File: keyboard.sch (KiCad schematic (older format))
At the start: 34 parts, among them J1 USB_C_Receptacle_USB2.0, J2 -, J3 -, K1 SW, K2 SW, P1 SWD, P2 BATT, P3 BATT, U1 nRF52810-ND04C, U2 CH554T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

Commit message: 更新部分cache的库
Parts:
- R1, R101, R102, R103, R2, R3, R4, R5, R6: symbol keyboard-rescue:R_Small-RESCUE-ble4100-nrf-ble4100-nrf-rescue -> Device:R_Small
- U2: symbol keyboard-rescue:CH554T-ch554t -> custom:CH554T
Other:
- moved on the sheet: C1, C2, J1, K1, P1, R1, R5, R6

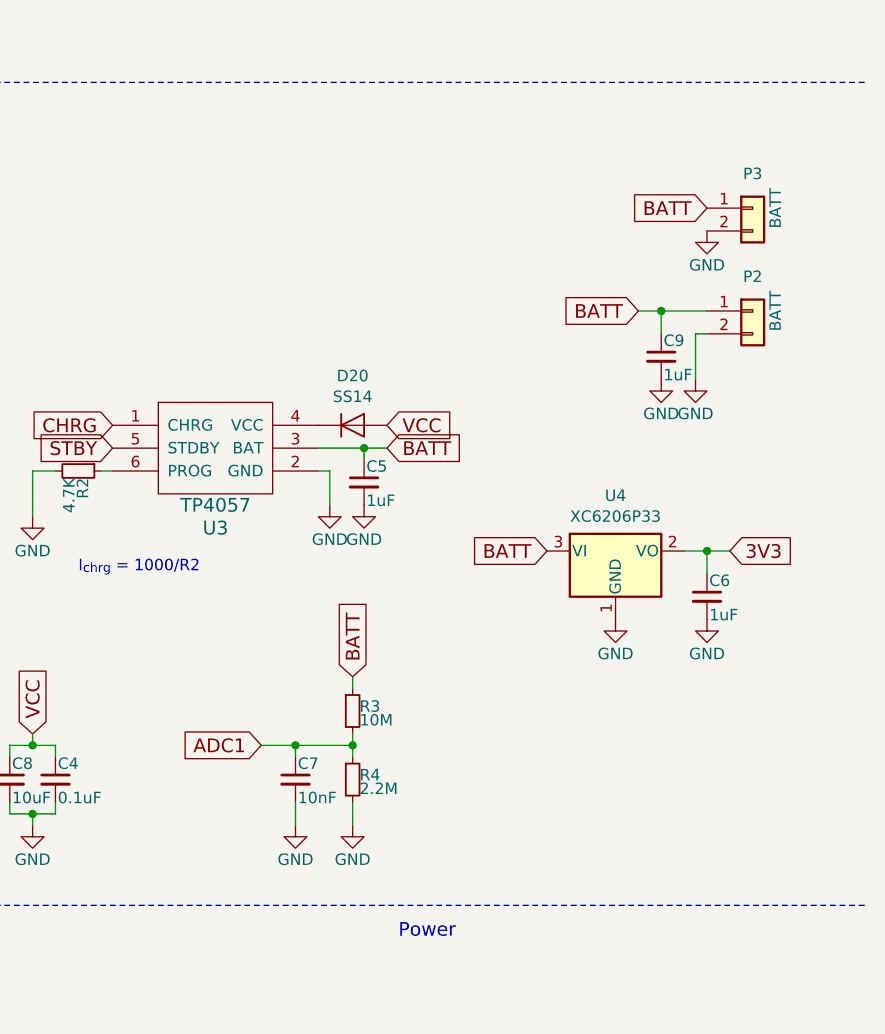
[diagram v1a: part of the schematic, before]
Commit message: 改进供电部分，现在支持仅USB供电了
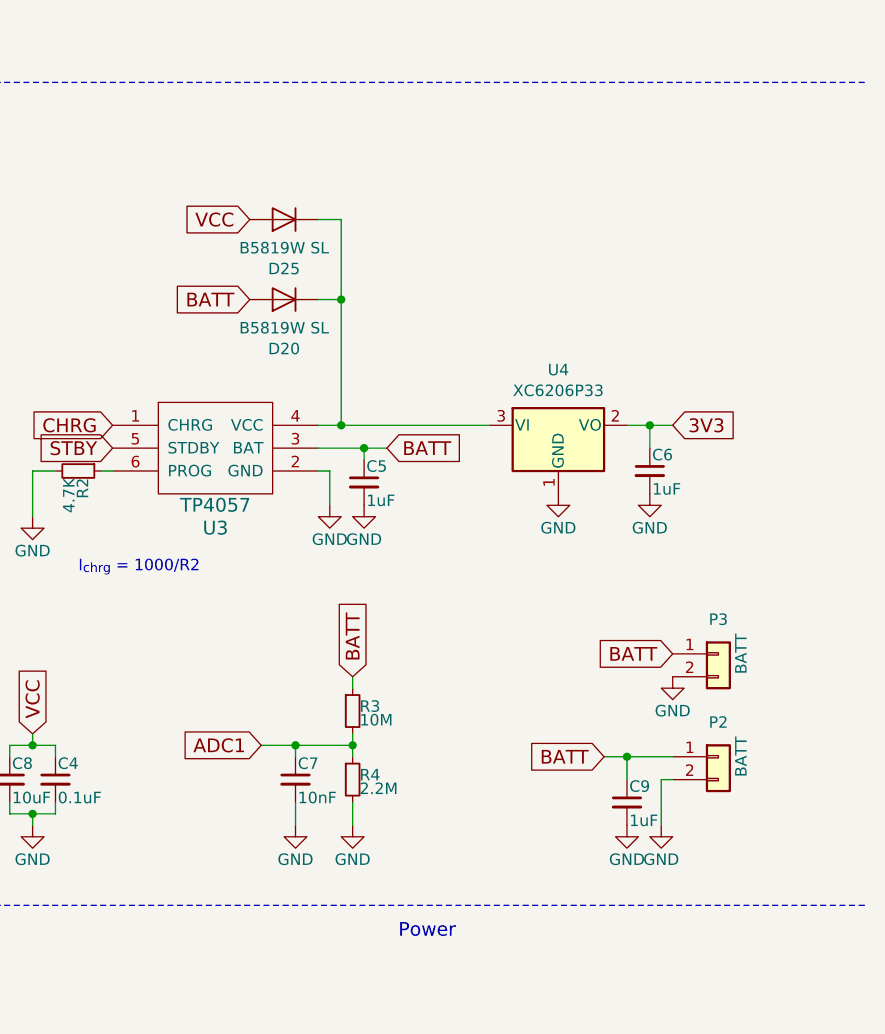
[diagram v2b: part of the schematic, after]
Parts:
- added D25: B5819W SL, Diode_SMD:D_SOD-123, symbol Device:D
- D20: value SS14 -> B5819W SL; footprint Diode_SMD:D_SMA -> Diode_SMD:D_SOD-123
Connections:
- net BATT: now also D20.2 (A); no longer U4.3 (VI)
- net VCC: now also D25.2 (A); no longer D20.2 (A)
- net at D20.1 (K), U3.4 (VCC): now also U4.3 (VI), D25.1 (K)
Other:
- moved on the sheet: C6, C9, D20, P2, P3, U4
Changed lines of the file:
@@
 L Connector_Generic:Conn_01x02 P2
 U 1 1 5867EF56
-P 10700 3700
-F 0 "P2" H 10700 3850 50  0000 C CNN
-F 1 "BATT" V 10800 3700 50  0000 C CNN
-F 2 "Connector_PinHeader_2.54mm:PinHeader_1x02_P2.54mm_Vertical" H 10700 3700 50  0001 C CNN
-F 3 "" H 10700 3700 50  0000 C CNN
-	1    10700 3700
+P 10550 5650
+F 0 "P2" H 10550 5800 50  0000 C CNN
+F 1 "BATT" V 10650 5650 50  0000 C CNN
+F 2 "Connector_PinHeader_2.54mm:PinHeader_1x02_P2.54mm_Vertical" H 10550 5650 50  0001 C CNN
+F 3 "" H 10550 5650 50  0000 C CNN
+	1    10550 5650
 	1    0    0    -1
 $EndComp
@@
 L power:GND #PWR017
 U 1 1 58688C41
-P 10450 4000
-F 0 "#PWR017" H 10450 3750 50  0001 C CNN
-F 1 "GND" H 10450 3850 50  0000 C CNN
-F 2 "" H 10450 4000 50  0000 C CNN
-F 3 "" H 10450 4000 50  0000 C CNN
-	1    10450 4000
+P 10300 5950
+F 0 "#PWR017" H 10300 5700 50  0001 C CNN
+F 1 "GND" H 10300 5800 50  0000 C CNN
+F 2 "" H 10300 5950 50  0000 C CNN
+F 3 "" H 10300 5950 50  0000 C CNN
+	1    10300 5950
 	1    0    0    -1
 $EndComp
 Text GLabel 9100 4300 2    60   Input ~ 0
 BATT
-Text GLabel 10200 3700 0    60   Input ~ 0
+Text GLabel 10050 5650 0    60   Input ~ 0
 BATT
 Text GLabel 1300 4650 2    60   Input ~ 0
@@
 L Device:C_Small C6
 U 1 1 58689C99
-P 10500 4950
-F 0 "C6" H 10510 5020 50  0000 L CNN
-F 1 "1uF" H 10510 4870 50  0000 L CNN
-F 2 "Capacitor_SMD:C_0805_2012Metric" H 10500 4950 50  0001 C CNN
-F 3 "~" H 10500 4950 50  0000 C CNN
-	1    10500 4950
+P 10250 4400
+F 0 "C6" H 10260 4470 50  0000 L CNN
+F 1 "1uF" H 10260 4320 50  0000 L CNN
+F 2 "Capacitor_SMD:C_0805_2012Metric" H 10250 4400 50  0001 C CNN
+F 3 "~" H 10250 4400 50  0000 C CNN
+	1    10250 4400
 	1    0    0    -1
 $EndComp
@@
 Text Notes 9150 6450 0    60   ~ 0
 Power
-Text GLabel 9100 4200 2    60   Input ~ 0
+Text GLabel 8500 3300 0    60   Input ~ 0
 VCC
 Text GLabel 7550 5550 1    60   Input ~ 0
@@
 	8850 4400 8850 4550
 Wire Wire Line
-	10500 3800 10450 3800
-Wire Wire Line
-	10450 3800 10450 4000
+	10350 5750 10300 5750
+Wire Wire Line
+	10300 5750 10300 5950
 Wire Wire Line
 	1300 4350 1400 4350
@@
 L Regulator_Linear:AP2127N-3.0 U4
 U 1 1 5AE6D677
-P 10100 4750
-F 0 "U4" H 10100 4992 50  0000 C CNN
-F 1 "XC6206P33" H 10100 4901 50  0000 C CNN
-F 2 "Package_TO_SOT_SMD:SOT-23" H 10100 4975 50  0001 C CIN
-F 3 "https://www.diodes.com/assets/Datasheets/AP2127.pdf" H 10100 4750 50  0001 C CNN
-	1    10100 4750
-	1    0    0    -1
-$EndComp
-Text GLabel 9800 4750 0    60   Input ~ 0
-BATT
-Text GLabel 10600 4750 2    60   Input ~ 0
+P 9850 4200
+F 0 "U4" H 9850 4442 50  0000 C CNN
+F 1 "XC6206P33" H 9850 4351 50  0000 C CNN
+F 2 "Package_TO_SOT_SMD:SOT-23" H 9850 4425 50  0001 C CIN
+F 3 "https://www.diodes.com/assets/Datasheets/AP2127.pdf" H 9850 4200 50  0001 C CNN
+	1    9850 4200
+	1    0    0    -1
+$EndComp
+Text GLabel 10350 4200 2    60   Input ~ 0
 3V3
 $Comp
 L power:GND #PWR016
 U 1 1 5AE6D8BF
-P 10100 5050
-F 0 "#PWR016" H 10100 4800 50  0001 C CNN
-F 1 "GND" H 10100 4900 50  0000 C CNN
-F 2 "" H 10100 5050 50  0000 C CNN
-F 3 "" H 10100 5050 50  0000 C CNN
-	1    10100 5050
+P 9850 4500
+F 0 "#PWR016" H 9850 4250 50  0001 C CNN
+F 1 "GND" H 9850 4350 50  0000 C CNN
+F 2 "" H 9850 4500 50  0000 C CNN
+F 3 "" H 9850 4500 50  0000 C CNN
+	1    9850 4500
 	1    0    0    -1
 $EndComp
@@
 L Device:D D20
 U 1 1 5AFFEAFC
-P 8950 4200
-F 0 "D20" H 8950 4416 50  0000 C CNN
-F 1 "SS14" H 8950 4325 50  0000 C CNN
-F 2 "Diode_SMD:D_SMA" H 8950 4200 50  0001 C CNN
-F 3 "~" H 8950 4200 50  0001 C CNN
-	1    8950 4200
-	1    0    0    -1
+P 8650 3650
+F 0 "D20" H 8650 3866 50  0000 C CNN
+F 1 "B5819W SL" H 8650 3775 50  0000 C CNN
+F 2 "Diode_SMD:D_SOD-123" H 8650 3650 50  0001 C CNN
+F 3 "~" H 8650 3650 50  0001 C CNN
+	1    8650 3650
+	-1   0    0    1
 $EndComp
 Text GLabel 2800 4100 2    60   Input ~ 0
@@
 L power:GND #PWR023
 U 1 1 5CC46D5E
-P 10500 5050
-F 0 "#PWR023" H 10500 4800 50  0001 C CNN
-F 1 "GND" H 10500 4900 50  0000 C CNN
-F 2 "" H 10500 5050 50  0000 C CNN
-F 3 "" H 10500 5050 50  0000 C CNN
-	1    10500 5050
-	1    0    0    -1
-$EndComp
-Wire Wire Line
-	10400 4750 10500 4750
-Wire Wire Line
-	10500 4850 10500 4750
-Connection ~ 10500 4750
-Wire Wire Line
-	10500 4750 10600 4750
+P 10250 4500
+F 0 "#PWR023" H 10250 4250 50  0001 C CNN
+F 1 "GND" H 10250 4350 50  0000 C CNN
+F 2 "" H 10250 4500 50  0000 C CNN
+F 3 "" H 10250 4500 50  0000 C CNN
+	1    10250 4500
+	1    0    0    -1
+$EndComp
+Wire Wire Line
+	10150 4200 10250 4200
+Wire Wire Line
+	10250 4300 10250 4200
+Connection ~ 10250 4200
+Wire Wire Line
+	10250 4200 10350 4200
 Wire Wire Line
 	8800 4300 9000 4300
@@
 $EndComp
 Wire Wire Line
-	10500 3700 10300 3700
+	10350 5650 10150 5650
 $Comp
 L Device:C_Small C9
 U 1 1 5CD13C66
-P 10300 3900
-F 0 "C9" H 10310 3970 50  0000 L CNN
-F 1 "1uF" H 10310 3820 50  0000 L CNN
-F 2 "Capacitor_SMD:C_0805_2012Metric" H 10300 3900 50  0001 C CNN
-F 3 "~" H 10300 3900 50  0000 C CNN
-	1    10300 3900
-	1    0    0    -1
-$EndComp
-Wire Wire Line
-	10300 3800 10300 3700
-Connection ~ 10300 3700
-Wire Wire Line
-	10300 3700 10200 3700
+P 10150 5850
+F 0 "C9" H 10160 5920 50  0000 L CNN
+F 1 "1uF" H 10160 5770 50  0000 L CNN
+F 2 "Capacitor_SMD:C_0805_2012Metric" H 10150 5850 50  0001 C CNN
+F 3 "~" H 10150 5850 50  0000 C CNN
+	1    10150 5850
+	1    0    0    -1
+$EndComp
+Wire Wire Line
+	10150 5750 10150 5650
+Connection ~ 10150 5650
+Wire Wire Line
+	10150 5650 10050 5650
 $Comp
 L power:GND #PWR012
 U 1 1 5CD4AD12
-P 10300 4000
-F 0 "#PWR012" H 10300 3750 50  0001 C CNN
-F 1 "GND" H 10300 3850 50  0000 C CNN
-F 2 "" H 10300 4000 50  0000 C CNN
-F 3 "" H 10300 4000 50  0000 C CNN
-	1    10300 4000
+P 10150 5950
+F 0 "#PWR012" H 10150 5700 50  0001 C CNN
+F 1 "GND" H 10150 5800 50  0000 C CNN
+F 2 "" H 10150 5950 50  0000 C CNN
+F 3 "" H 10150 5950 50  0000 C CNN
+	1    10150 5950
 	1    0    0    -1
 $EndComp
@@
 L Connector_Generic:Conn_01x02 P3
 U 1 1 5D6C74C7
-P 10700 3250
-F 0 "P3" H 10700 3400 50  0000 C CNN
-F 1 "BATT" V 10800 3250 50  0000 C CNN
-F 2 "Connector_PinSocket_2.00mm:PinSocket_1x02_P2.00mm_Vertical" H 10700 3250 50  0001 C CNN
-F 3 "" H 10700 3250 50  0000 C CNN
-	1    10700 3250
-	1    0    0    -1
-$EndComp
-Text GLabel 10500 3250 0    60   Input ~ 0
+P 10550 5200
+F 0 "P3" H 10550 5350 50  0000 C CNN
+F 1 "BATT" V 10650 5200 50  0000 C CNN
+F 2 "Connector_PinSocket_2.00mm:PinSocket_1x02_P2.00mm_Vertical" H 10550 5200 50  0001 C CNN
+F 3 "" H 10550 5200 50  0000 C CNN
+	1    10550 5200
+	1    0    0    -1
+$EndComp
+Text GLabel 10350 5200 0    60   Input ~ 0
 BATT
 $Comp
 L power:GND #PWR0101
 U 1 1 5D6C7B4E
-P 10500 3350
-F 0 "#PWR0101" H 10500 3100 50  0001 C CNN
-F 1 "GND" H 10500 3200 50  0000 C CNN
-F 2 "" H 10500 3350 50  0000 C CNN
-F 3 "" H 10500 3350 50  0000 C CNN
-	1    10500 3350
-	1    0    0    -1
-$EndComp
+P 10350 5300
+F 0 "#PWR0101" H 10350 5050 50  0001 C CNN
+F 1 "GND" H 10350 5150 50  0000 C CNN
+F 2 "" H 10350 5300 50  0000 C CNN
+F 3 "" H 10350 5300 50  0000 C CNN
+	1    10350 5300
+	1    0    0    -1
+$EndComp
+$Comp
+L Device:D D25
+U 1 1 5E0ABEC8
+P 8650 3300
+F 0 "D25" H 8650 3516 50  0000 C CNN
+F 1 "B5819W SL" H 8650 3425 50  0000 C CNN
+F 2 "Diode_SMD:D_SOD-123" H 8650 3300 50  0001 C CNN
+F 3 "~" H 8650 3300 50  0001 C CNN
+	1    8650 3300
+	-1   0    0    1
+$EndComp
+Text GLabel 8500 3650 0    60   Input ~ 0
+BATT
+Wire Wire Line
+	8800 3300 8900 3300
+Wire Wire Line
+	8900 3300 8900 3650
+Wire Wire Line
+	8900 3650 8800 3650
+Wire Wire Line
+	8900 3650 8900 4200
+Wire Wire Line
+	8900 4200 8800 4200
+Connection ~ 8900 3650
+Wire Wire Line
+	8900 4200 9550 4200
+Connection ~ 8900 4200
 Wire Bus Line
 	2100 1250 3850 1250
